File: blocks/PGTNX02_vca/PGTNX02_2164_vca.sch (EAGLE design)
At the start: 77 parts, among them IC1 79L05, IC2 V2164, IC3 TL074P

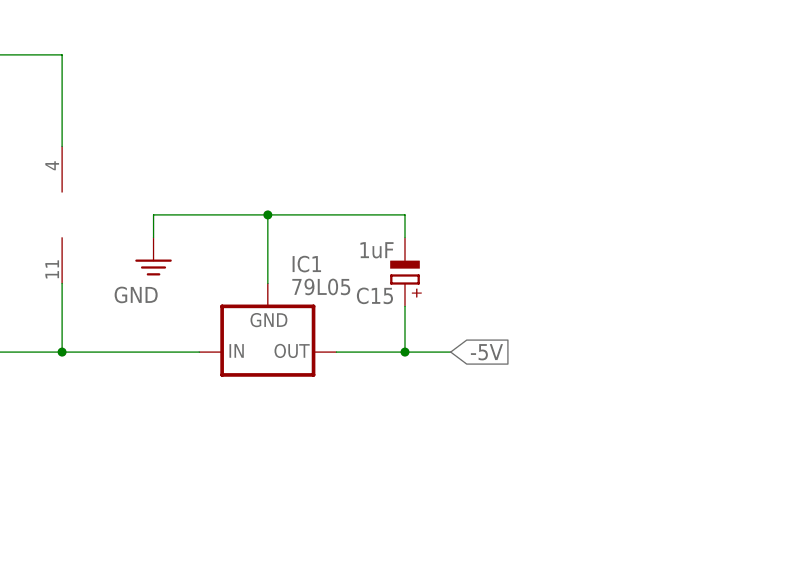
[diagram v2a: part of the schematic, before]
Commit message: Corrected Polarity of C15
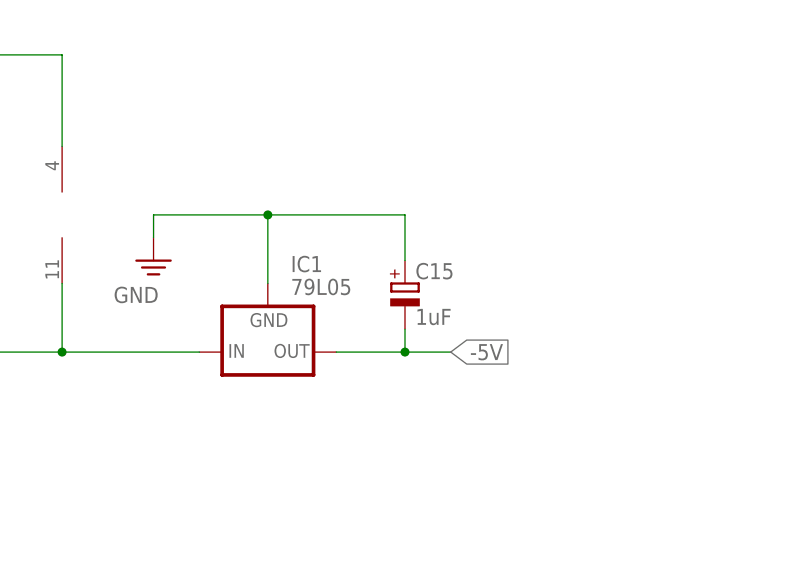
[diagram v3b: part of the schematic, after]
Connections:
- net -5V: now also C15.-; no longer C15.+
- net PE: now also C15.+; no longer C15.-
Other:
- moved on the sheet: C15
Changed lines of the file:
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@@
 <attribute name="VALUE" x="99.06" y="69.85" size="1.778" layer="96"/>
 </instance>
-<instance part="C15" gate="G$1" x="111.76" y="71.12" smashed="yes" rot="R180">
-<attribute name="NAME" x="110.617" y="70.6374" size="1.778" layer="95" rot="R180"/>
-<attribute name="VALUE" x="110.617" y="75.7174" size="1.778" layer="96" rot="R180"/>
+<instance part="C15" gate="G$1" x="111.76" y="71.12" smashed="yes">
+<attribute name="NAME" x="112.903" y="71.6026" size="1.778" layer="95"/>
+<attribute name="VALUE" x="112.903" y="66.5226" size="1.778" layer="96"/>
 </instance>
 <instance part="SUPPLY19" gate="GND" x="83.82" y="73.66" smashed="yes">
@@
 </segment>
 <segment>
-<pinref part="C15" gate="G$1" pin="-"/>
-<wire x1="111.76" y1="76.2" x2="111.76" y2="78.74" width="0.1524" layer="91"/>
 <pinref part="IC1" gate="A" pin="GND"/>
 <wire x1="111.76" y1="78.74" x2="96.52" y2="78.74" width="0.1524" layer="91"/>
@@
 <pinref part="SUPPLY19" gate="GND" pin="PE"/>
 <wire x1="83.82" y1="78.74" x2="83.82" y2="76.2" width="0.1524" layer="91"/>
+<pinref part="C15" gate="G$1" pin="+"/>
+<wire x1="111.76" y1="73.66" x2="111.76" y2="78.74" width="0.1524" layer="91"/>
 </segment>
 <segment>
@@
 <wire x1="104.14" y1="63.5" x2="111.76" y2="63.5" width="0.1524" layer="91"/>
 <label x="116.84" y="63.5" size="1.778" layer="95" xref="yes"/>
-<pinref part="C15" gate="G$1" pin="+"/>
+<pinref part="C15" gate="G$1" pin="-"/>
 <wire x1="111.76" y1="63.5" x2="116.84" y2="63.5" width="0.1524" layer="91"/>
-<wire x1="111.76" y1="68.58" x2="111.76" y2="63.5" width="0.1524" layer="91"/>
+<wire x1="111.76" y1="66.04" x2="111.76" y2="63.5" width="0.1524" layer="91"/>
 <junction x="111.76" y="63.5"/>
 </segment>
